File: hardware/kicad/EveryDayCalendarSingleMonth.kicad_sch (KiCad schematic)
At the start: 138 parts, among them J2_POWER_IN1 Conn_01x02, J3_PROGRAMING_PIN1 Conn_01x06, Q1 PN2222A, Q2 PN2222A, U1 74AHC1G125

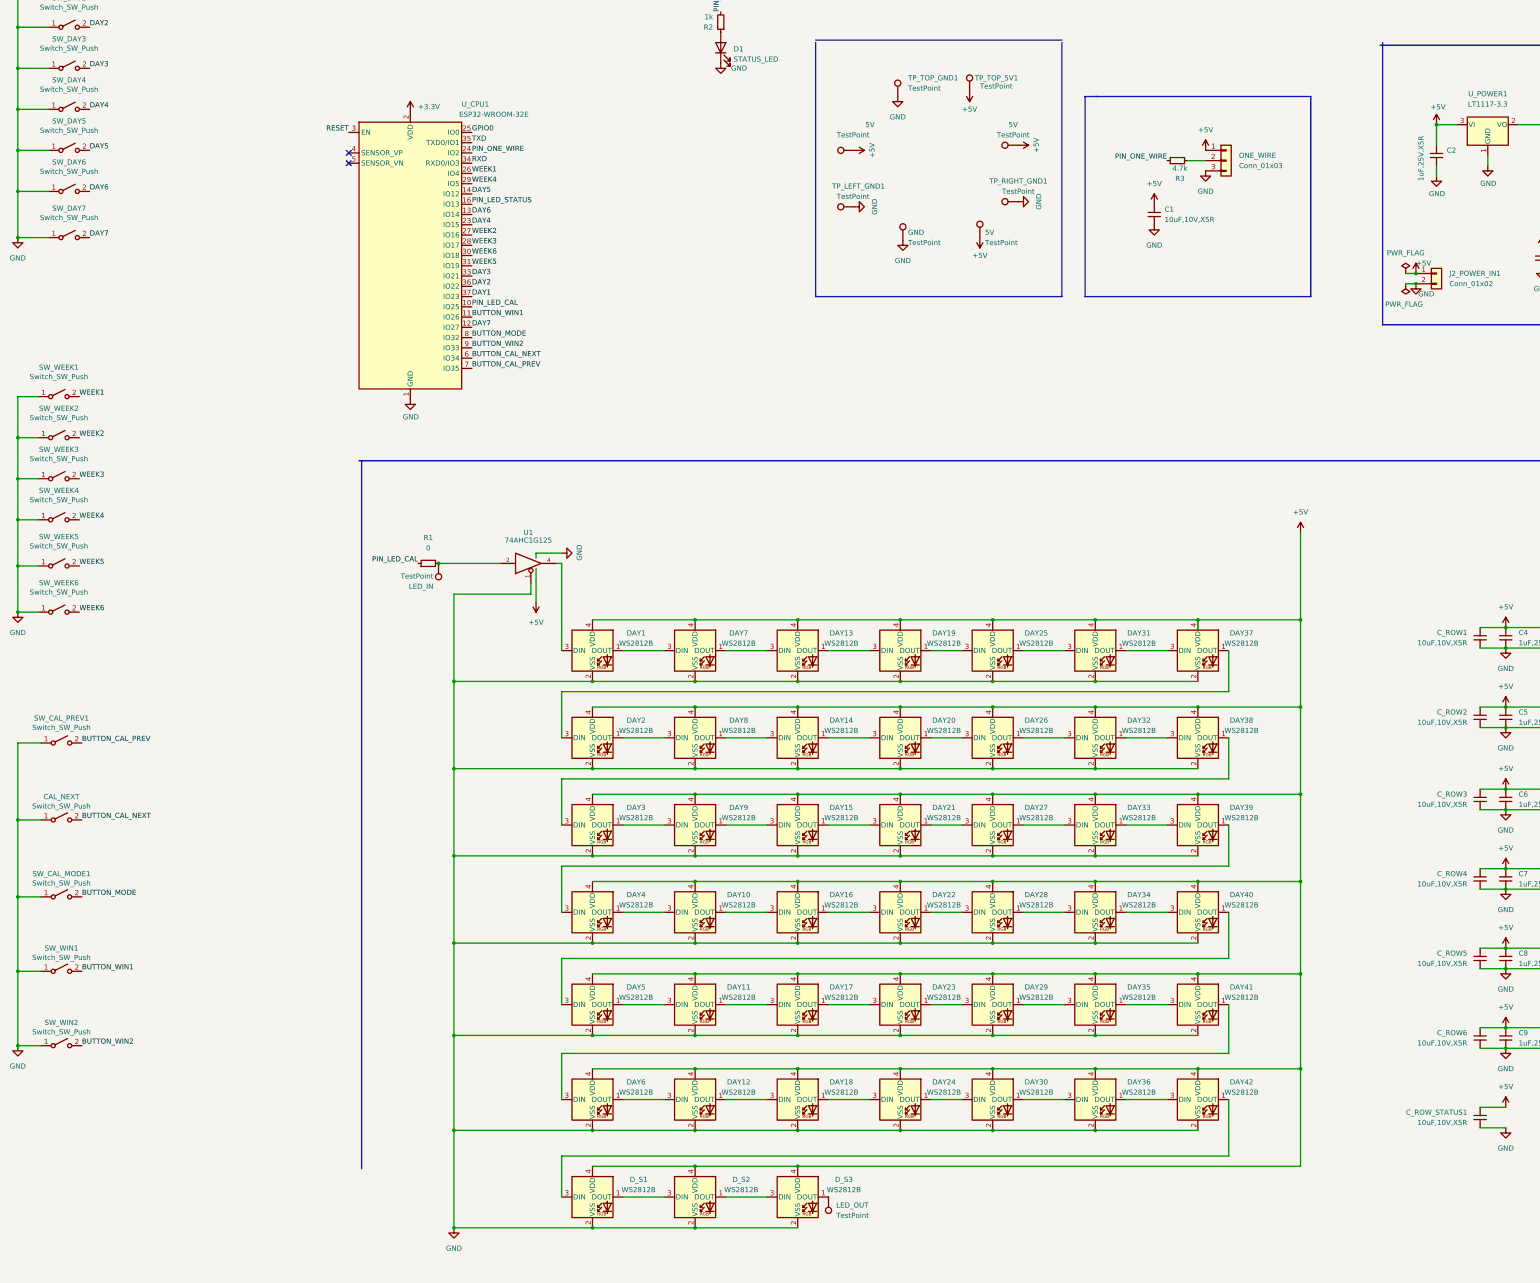
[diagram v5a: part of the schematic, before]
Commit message: Updated the schematic from PCB layout with updated silkscreen
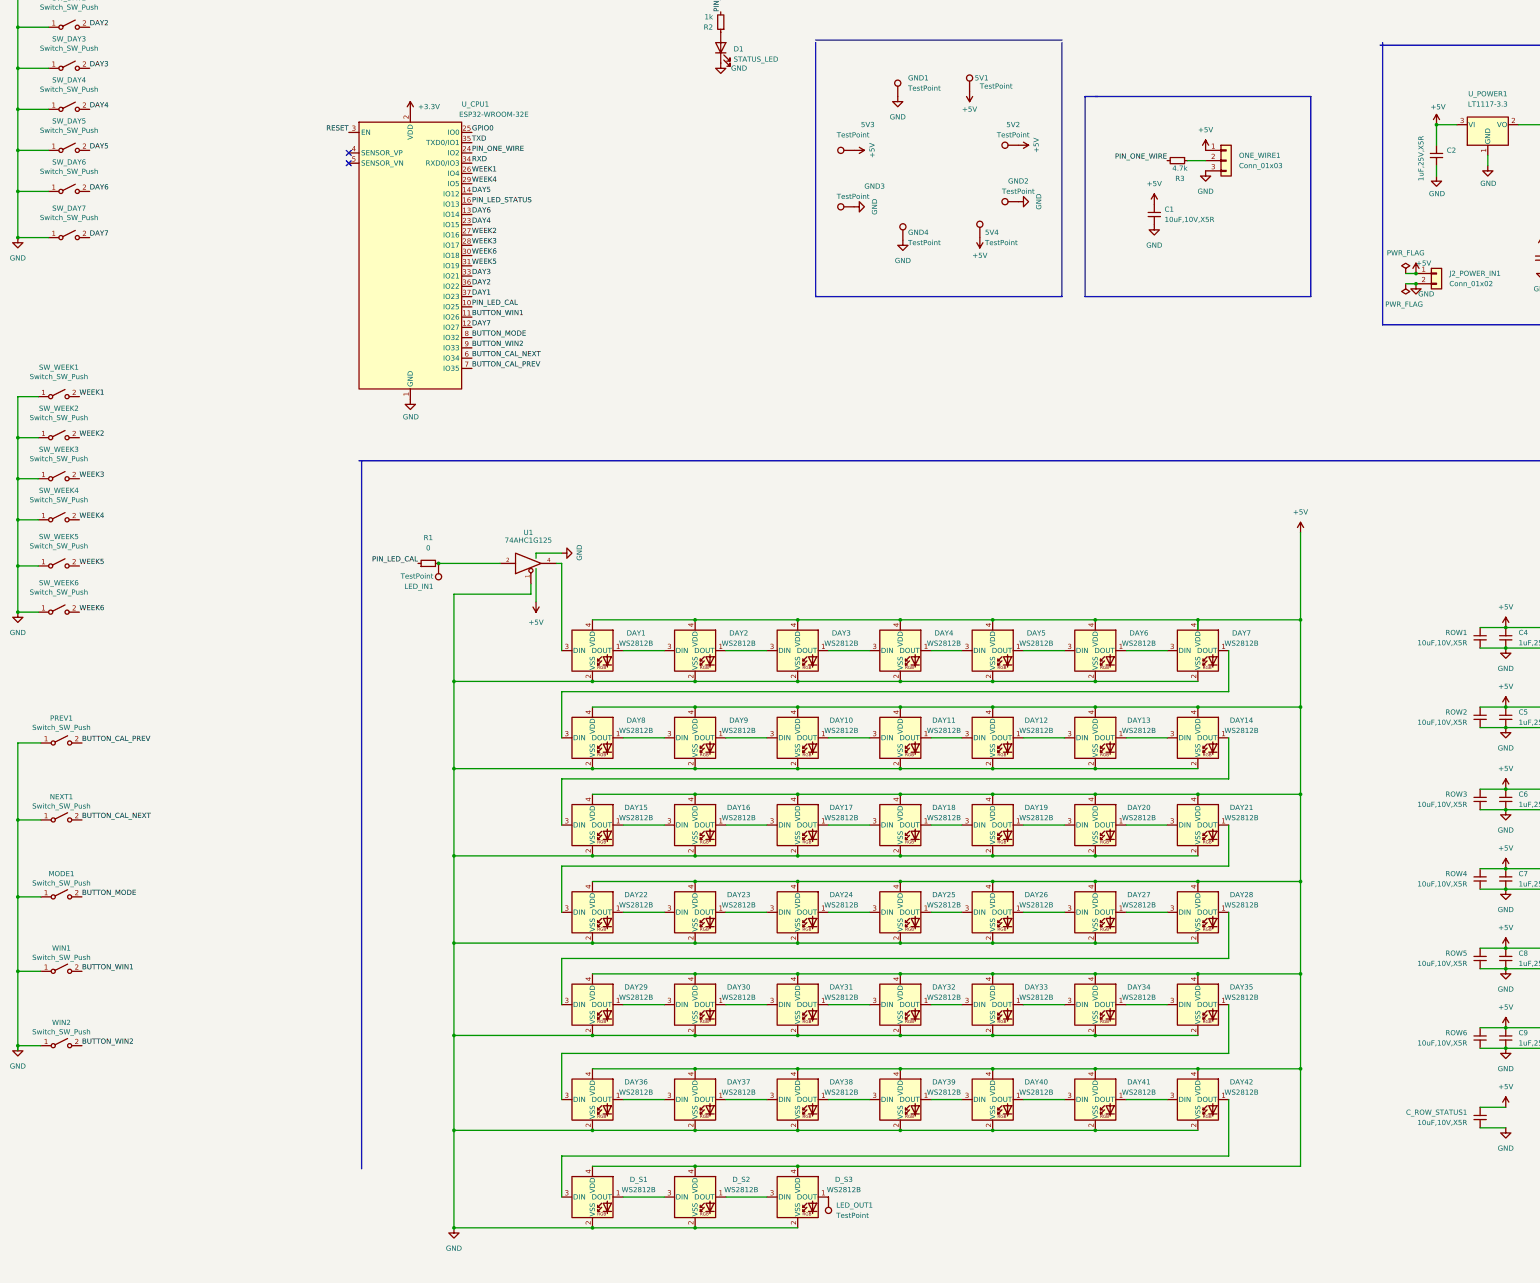
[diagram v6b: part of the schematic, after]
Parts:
- renumbered TP_TOP_5V1 to 5V1, 5V to 5V2, 5V to 5V3, 5V to 5V4, DAY14 to DAY10, DAY20 to DAY11, DAY26 to DAY12, DAY32 to DAY13, DAY38 to DAY14, DAY3 to DAY15, DAY9 to DAY16, DAY15 to DAY17, DAY21 to DAY18, DAY27 to DAY19, DAY7 to DAY2, DAY33 to DAY20, DAY39 to DAY21, DAY4 to DAY22, DAY10 to DAY23, DAY16 to DAY24, DAY22 to DAY25, DAY28 to DAY26, DAY34 to DAY27, DAY40 to DAY28, DAY5 to DAY29, DAY13 to DAY3, DAY11 to DAY30, DAY17 to DAY31, DAY23 to DAY32, DAY29 to DAY33, DAY35 to DAY34, DAY41 to DAY35, DAY6 to DAY36, DAY12 to DAY37, DAY18 to DAY38, DAY24 to DAY39, DAY19 to DAY4, DAY30 to DAY40, DAY36 to DAY41, DAY25 to DAY5, DAY31 to DAY6, DAY37 to DAY7, DAY2 to DAY8, DAY8 to DAY9, TP_TOP_GND1 to GND1, TP_RIGHT_GND1 to GND2, TP_LEFT_GND1 to GND3, GND to GND4, LED_IN to LED_IN1, LED_OUT to LED_OUT1, SW_CAL_MODE1 to MODE1, CAL_NEXT to NEXT1, ONE_WIRE to ONE_WIRE1, SW_CAL_PREV1 to PREV1, C_ROW1 to ROW1, C_ROW2 to ROW2, C_ROW3 to ROW3, C_ROW4 to ROW4, C_ROW5 to ROW5, C_ROW6 to ROW6, SW_WIN1 to WIN1, SW_WIN2 to WIN2

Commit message: Fussing with the tracks, no real change
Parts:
- added TP_CAL_NEXT1, TP_CAL_PREV1, TP_MODE1, TP_WIN1, TP_WIN2: TestPoint, TestPoint:TestPoint_Pad_2.5x2.5mm, symbol Connector:TestPoint
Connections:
- net BUTTON_CAL_NEXT: now also TP_CAL_NEXT1.1
- net BUTTON_CAL_PREV: now also TP_CAL_PREV1.1
- net BUTTON_MODE: now also TP_MODE1.1
- net BUTTON_WIN1: now also TP_WIN1.1
- net BUTTON_WIN2: now also TP_WIN2.1
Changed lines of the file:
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@@
     (pin "2")
   )
+  (symbol (lib_id "Connector:TestPoint") (at 41.275 274.32 180) (unit 1)
+    (in_bom yes) (on_board yes) (fields_autoplaced)
+    (property "Reference" "TP_WIN1" (id 0) (at 43.18 276.3519 0)
+      (effects (font (size 1.27 1.27)) (justify right))
+    )
+    (property "Value" "TestPoint" (id 1) (at 43.18 278.8919 0)
+      (effects (font (size 1.27 1.27)) (justify right))
+    )
+    (property "Footprint" "TestPoint:TestPoint_Pad_2.5x2.5mm" (id 2) (at 36.195 274.32 0)
+      (effects (font (size 1.27 1.27)) hide)
+    )
+    (property "Datasheet" "~" (id 3) (at 36.195 274.32 0)
+      (effects (font (size 1.27 1.27)) hide)
+    )
+    (pin "1")
+  )
   (symbol (lib_id "calendar:WS2812B") (at 167.64 330.2 0) (unit 1)
     (in_bom yes) (on_board yes) (fields_autoplaced)
@@
     (pin "1")
   )
+  (symbol (lib_id "Connector:TestPoint") (at 41.275 236.855 180) (unit 1)
+    (in_bom yes) (on_board yes) (fields_autoplaced)
+    (property "Reference" "TP_CAL_NEXT1" (id 0) (at 43.18 238.8869 0)
+      (effects (font (size 1.27 1.27)) (justify right))
+    )
+    (property "Value" "TestPoint" (id 1) (at 43.18 241.4269 0)
+      (effects (font (size 1.27 1.27)) (justify right))
+    )
+    (property "Footprint" "TestPoint:TestPoint_Pad_2.5x2.5mm" (id 2) (at 36.195 236.855 0)
+      (effects (font (size 1.27 1.27)) hide)
+    )
+    (property "Datasheet" "~" (id 3) (at 36.195 236.855 0)
+      (effects (font (size 1.27 1.27)) hide)
+    )
+    (pin "1")
+  )
   (symbol (lib_id "power:GND") (at 133.35 337.82 0) (unit 1)
     (in_bom yes) (on_board yes) (fields_autoplaced)
@@
     (pin "2")
   )
+  (symbol (lib_id "Connector:TestPoint") (at 41.275 217.805 180) (unit 1)
+    (in_bom yes) (on_board yes) (fields_autoplaced)
+    (property "Reference" "TP_CAL_PREV1" (id 0) (at 43.18 219.8369 0)
+      (effects (font (size 1.27 1.27)) (justify right))
+    )
+    (property "Value" "TestPoint" (id 1) (at 43.18 222.3769 0)
+      (effects (font (size 1.27 1.27)) (justify right))
+    )
+    (property "Footprint" "TestPoint:TestPoint_Pad_2.5x2.5mm" (id 2) (at 36.195 217.805 0)
+      (effects (font (size 1.27 1.27)) hide)
+    )
+    (property "Datasheet" "~" (id 3) (at 36.195 217.805 0)
+      (effects (font (size 1.27 1.27)) hide)
+    )
+    (pin "1")
+  )
   (symbol (lib_id "calendar:WS2812B") (at 292.1 306.07 0) (unit 1)
     (in_bom yes) (on_board yes) (fields_autoplaced)
@@
     (pin "2")
   )
+  (symbol (lib_id "Connector:TestPoint") (at 41.275 292.735 180) (unit 1)
+    (in_bom yes) (on_board yes) (fields_autoplaced)
+    (property "Reference" "TP_WIN2" (id 0) (at 43.18 294.7669 0)
+      (effects (font (size 1.27 1.27)) (justify right))
+    )
+    (property "Value" "TestPoint" (id 1) (at 43.18 297.3069 0)
+      (effects (font (size 1.27 1.27)) (justify right))
+    )
+    (property "Footprint" "TestPoint:TestPoint_Pad_2.5x2.5mm" (id 2) (at 36.195 292.735 0)
+      (effects (font (size 1.27 1.27)) hide)
+    )
+    (property "Datasheet" "~" (id 3) (at 36.195 292.735 0)
+      (effects (font (size 1.27 1.27)) hide)
+    )
+    (pin "1")
+  )
+  (symbol (lib_id "Connector:TestPoint") (at 41.275 255.905 180) (unit 1)
+    (in_bom yes) (on_board yes) (fields_autoplaced)
+    (property "Reference" "TP_MODE1" (id 0) (at 43.18 257.9369 0)
+      (effects (font (size 1.27 1.27)) (justify right))
+    )
+    (property "Value" "TestPoint" (id 1) (at 43.18 260.4769 0)
+      (effects (font (size 1.27 1.27)) (justify right))
+    )
+    (property "Footprint" "TestPoint:TestPoint_Pad_2.5x2.5mm" (id 2) (at 36.195 255.905 0)
+      (effects (font (size 1.27 1.27)) hide)
+    )
+    (property "Datasheet" "~" (id 3) (at 36.195 255.905 0)
+      (effects (font (size 1.27 1.27)) hide)
+    )
+    (pin "1")
+  )
   (symbol (lib_id "calendar:WS2812B") (at 292.1 259.715 0) (unit 1)
     (in_bom yes) (on_board yes) (fields_autoplaced)
@@
       (reference "SW_WEEK6") (unit 1) (value "Switch_SW_Push") (footprint "calendar:SW_Push_1P1T_NO_6x6mm_H9.5mm")
     )
+    (path "/08be8f7a-9969-4b82-8d7f-20bf64b48847"
+      (reference "TP_CAL_NEXT1") (unit 1) (value "TestPoint") (footprint "TestPoint:TestPoint_Pad_2.5x2.5mm")
+    )
+    (path "/5f5e4afd-8693-41c1-a553-42f5106f491c"
+      (reference "TP_CAL_PREV1") (unit 1) (value "TestPoint") (footprint "TestPoint:TestPoint_Pad_2.5x2.5mm")
+    )
+    (path "/8201ec79-a5f7-42d7-9101-0cc4b5aa3062"
+      (reference "TP_MODE1") (unit 1) (value "TestPoint") (footprint "TestPoint:TestPoint_Pad_2.5x2.5mm")
+    )
+    (path "/06ced3eb-3535-4775-a23e-6fd8ccfb27d6"
+      (reference "TP_WIN1") (unit 1) (value "TestPoint") (footprint "TestPoint:TestPoint_Pad_2.5x2.5mm")
+    )
+    (path "/81ceff5c-8a17-4683-86dd-18baf50f401b"
+      (reference "TP_WIN2") (unit 1) (value "TestPoint") (footprint "TestPoint:TestPoint_Pad_2.5x2.5mm")
+    )
     (path "/80a94872-46d7-484e-9a3c-47123ec339d2"
